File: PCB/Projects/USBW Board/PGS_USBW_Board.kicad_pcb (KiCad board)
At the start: 4 copper layers, 50.8 x 32.6 mm, 44 parts, among them J1 Molex 505110-1792, J2 USB4056-03-A, J4 PH 2.0 JST, P1 RPI-RM2, Q1 BSS138DW, Q2 BSS138DW, U1 USBLC6-2P6, U2 USBLC6-2P6, U3 USBLC6-2P6, U4 TPS63001DRCR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

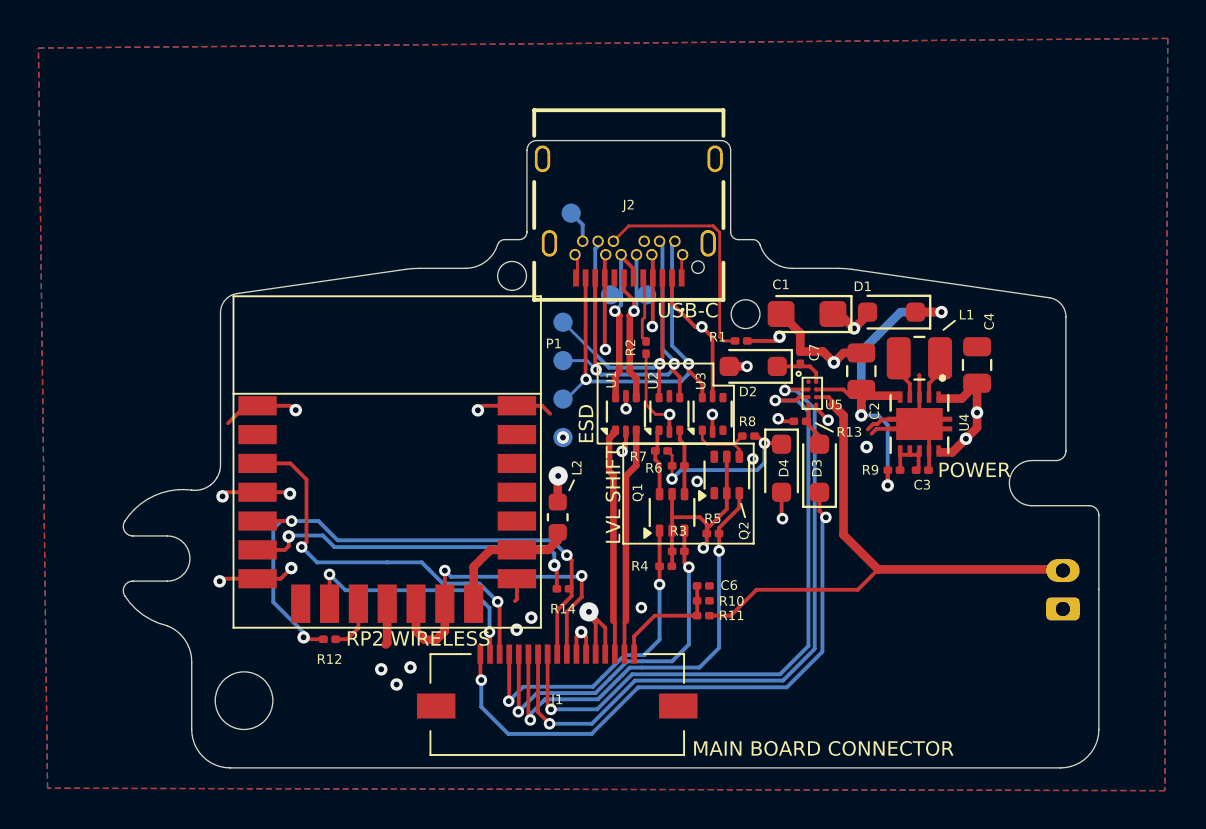
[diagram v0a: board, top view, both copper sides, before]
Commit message: USBW Update
- Implement fuel gauge IC
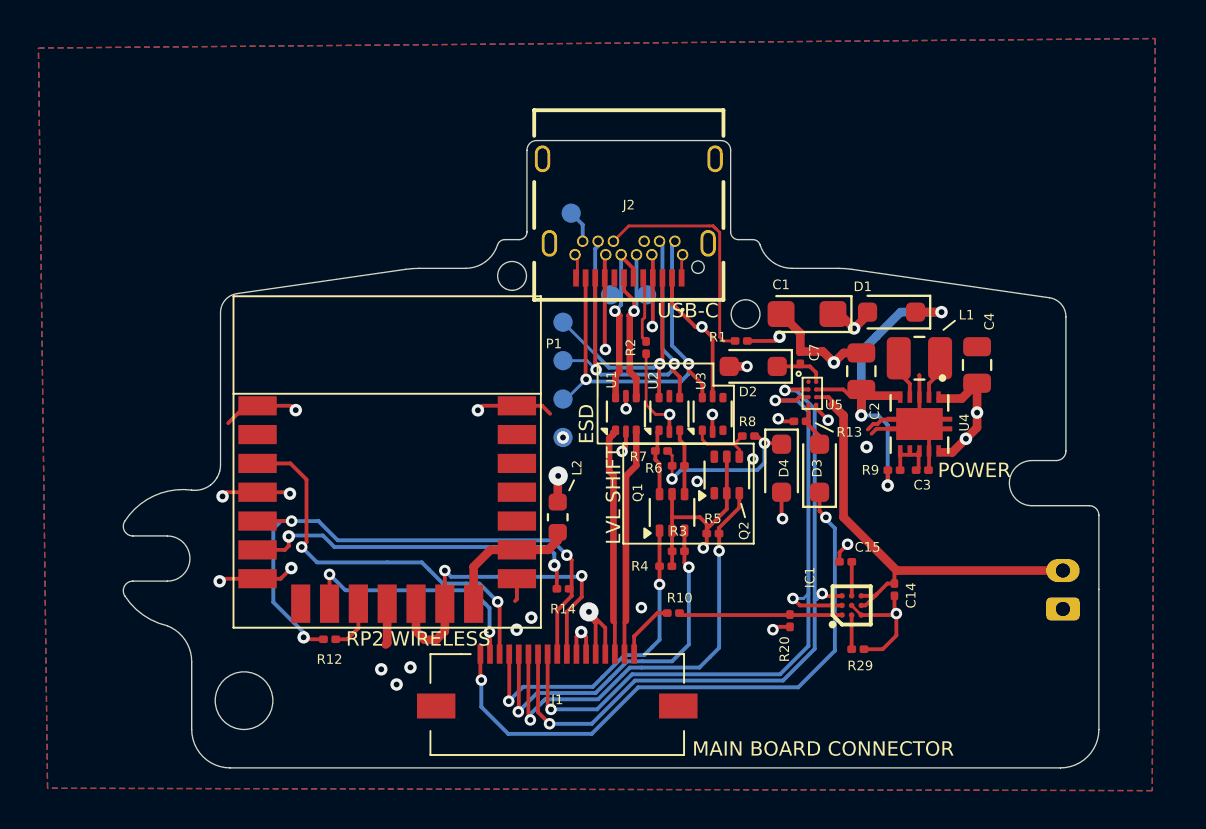
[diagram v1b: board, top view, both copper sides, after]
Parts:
- removed C6: 100nF, Capacitor_SMD:C_0201_0603Metric
- removed R11: 75k, Resistor_SMD:R_0201_0603Metric
- added C14: 1uF, Capacitor_SMD:C_0201_0603Metric, F.Cu at (80.9, 40.9)
- added C15: 0.47uF, Capacitor_SMD:C_0201_0603Metric, F.Cu at (78.4, 39.5)
- added IC1: BQ27621YZFR-G1A, hhl:BGA9C50P3X3_162X158X62, F.Cu at (78.7, 41.8)
- added R20: 10k, Resistor_SMD:R_0201_0603Metric, F.Cu at (75.5, 42.6)
- added R29: 10k, Resistor_SMD:R_0201_0603Metric, F.Cu at (79.0, 44.0)
- D1, D2, D3, D4: value CUS08F30,H3F -> CUS08F30,H3F
- R10: value 75k -> 0R
- moved R10 1.68 mm to (69.4, 42.2), turned to 0 degrees
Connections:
- R10 pad 1: GND -> BAT_LVL
- R10 pad 2: BAT_LVL -> BAT_MON_GPIO
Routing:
- net BAT_MON_GPIO: track 0.00 -> 8.50 mm
- net GND: track 51.6 -> 59.4 mm, vias 23 -> 25
- net BATTERY_POS: track 30.1 -> 23.6 mm
- net I2C1_SDA: track 33.7 -> 37.3 mm, vias 2 -> 3
- net BAT_LVL: track 6.20 -> 3.15 mm
- net Net-(IC1-BIN): track 0.00 -> 1.78 mm
- net Net-(IC1-VDD): track 0.00 -> 1.77 mm
- net I2C1_SCL: track 35.0 -> 36.6 mm, vias 2 -> 3
- net +3V3: track 26.0 -> 26.9 mm, vias 6 -> 7
- net BTN_PWR: track 31.4 -> 32.3 mm
